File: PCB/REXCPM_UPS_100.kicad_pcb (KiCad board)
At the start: 2 copper layers, 51.3 x 18.3 mm, 11 parts, among them J1 Model_100_System_BUS, J2 SM04B, U1 742G02

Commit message: replace BAT54C with BAV170 to protect batteries better
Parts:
- D1: value BAT54C -> BAV170
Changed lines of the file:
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@@
   (title_block
     (title "REXCPM_UPS_100")
-    (date "2023-09-18")
-    (rev "005")
+    (date "2023-09-21")
+    (rev "006")
     (company "Brian K. White - b.kenyon.w@gmail.com")
     (comment 1 "github.com/bkw777/REXCPM_UPS")
@@
         (effects (font (size 0.8 0.8) (thickness 0.1)) (justify mirror))
     )
-    (fp_text value "BAT54C" (at 3 -1.3 90 unlocked) (layer "B.SilkS")
+    (fp_text value "BAV170" (at 3 -1.3 90 unlocked) (layer "B.SilkS")
         (effects (font (size 0.8 0.8) (thickness 0.1)) (justify mirror))
     )
@@
     (fp_arc (start 4.905239 -2.551328) (mid 4.8 -2.952056) (end 4.906989 -3.352321)
       (stroke (width 0.1) (type default)) (layer "B.SilkS"))
-    (fp_arc (start 5.224755 -1.996844) (mid 5.280899 -1.852058) (end 5.3 -1.697943)
+    (fp_arc (start 5.224755 -1.996844) (mid 5.280909 -1.852057) (end 5.3 -1.697943)
       (stroke (width 0.1) (type default)) (layer "B.SilkS"))
     (fp_line (start -6.35 -1.6375) (end -6.35 1.6375)
@@
     (fp_arc (start 4.905239 -2.551328) (mid 4.8 -2.952056) (end 4.906989 -3.352321)
       (stroke (width 0.1) (type default)) (layer "B.SilkS"))
-    (fp_arc (start 5.224755 -1.996844) (mid 5.280899 -1.852058) (end 5.3 -1.697943)
+    (fp_arc (start 5.224755 -1.996844) (mid 5.280909 -1.852057) (end 5.3 -1.697943)
       (stroke (width 0.1) (type default)) (layer "B.SilkS"))
     (fp_line (start -6.35 -1.6375) (end -6.35 1.6375)
@@
     (fp_arc (start 4.905239 -2.551328) (mid 4.8 -2.952056) (end 4.906989 -3.352321)
       (stroke (width 0.1) (type default)) (layer "B.SilkS"))
-    (fp_arc (start 5.224755 -1.996844) (mid 5.280899 -1.852058) (end 5.3 -1.697943)
+    (fp_arc (start 5.224755 -1.996844) (mid 5.280909 -1.852057) (end 5.3 -1.697943)
       (stroke (width 0.1) (type default)) (layer "B.SilkS"))
     (fp_line (start -6.35 -1.6375) (end -6.35 1.6375)
@@
     (fp_arc (start 4.905239 -2.551328) (mid 4.8 -2.952056) (end 4.906989 -3.352321)
       (stroke (width 0.1) (type default)) (layer "B.SilkS"))
-    (fp_arc (start 5.224755 -1.996844) (mid 5.280913 -1.852059) (end 5.3 -1.697943)
+    (fp_arc (start 5.224755 -1.996844) (mid 5.280899 -1.852058) (end 5.3 -1.697943)
       (stroke (width 0.1) (type default)) (layer "B.SilkS"))
     (fp_line (start -6.35 -1.6375) (end -6.35 1.6375)

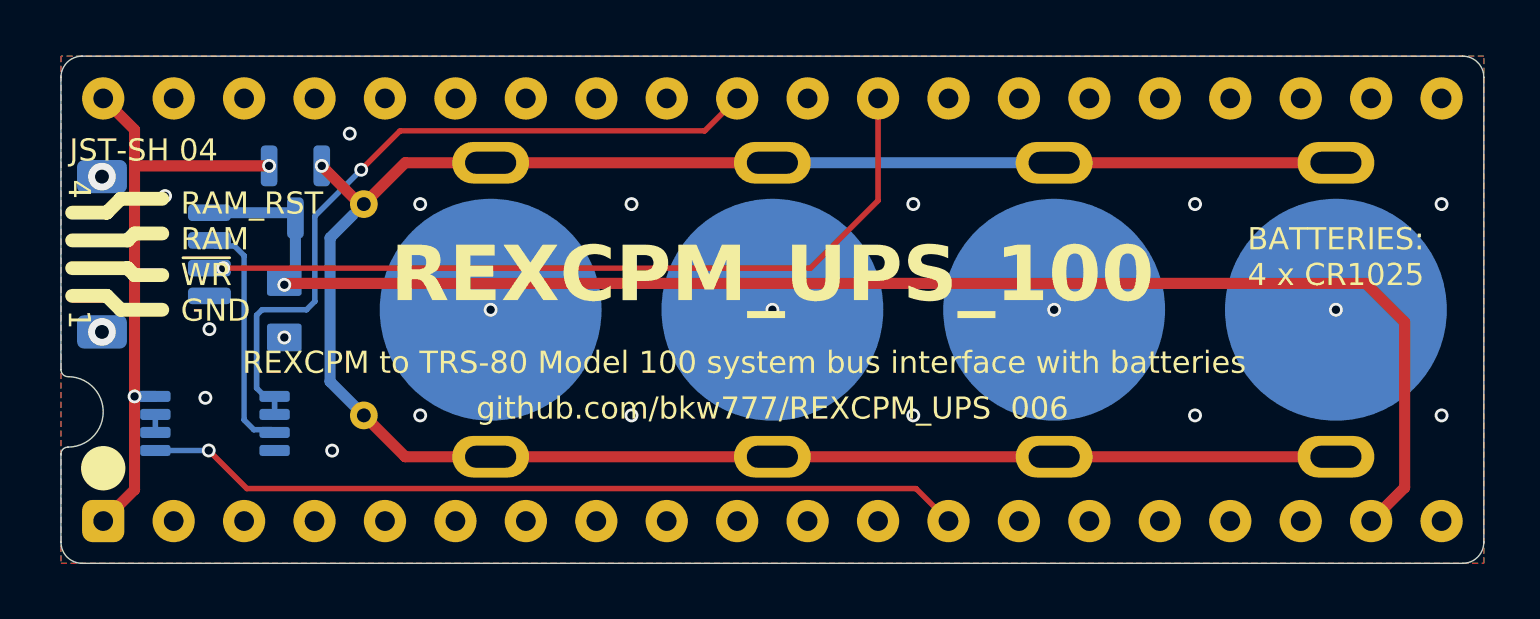
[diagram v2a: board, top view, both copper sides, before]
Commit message: m100 pcb routing, gnd, fiducials
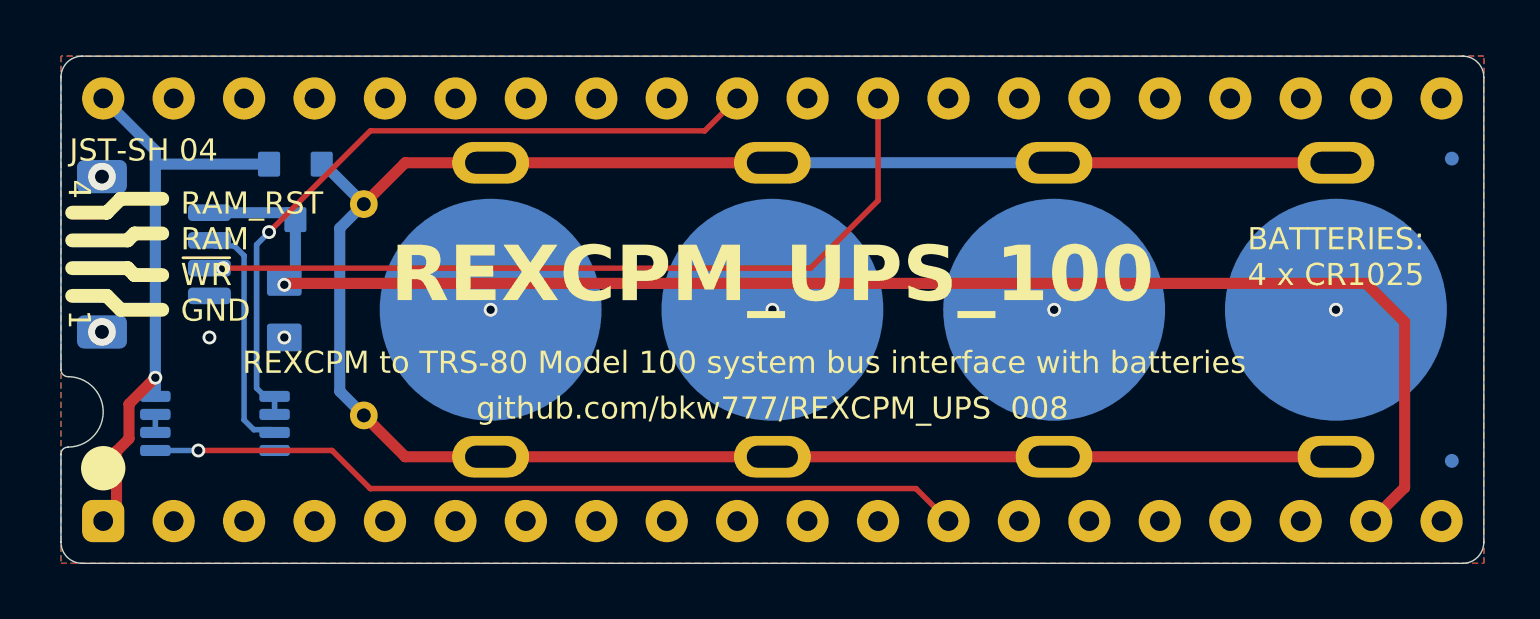
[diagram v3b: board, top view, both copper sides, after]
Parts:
- added REF**: Fiducial_0.5_1.0, 000_LOCAL:Fiducial_0.5_1.0, B.Cu at (112.6, 110.2)
- added REF**: Fiducial_0.5_1.0, 000_LOCAL:Fiducial_0.5_1.0, B.Cu at (161.0, 99.3)
- added REF**: Fiducial_0.5_1.0, 000_LOCAL:Fiducial_0.5_1.0, B.Cu at (161.0, 110.2)
- D1: footprint Package_TO_SOT_SMD:SOT-23 -> 000_LOCAL:SOT-23
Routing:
- net VBUS: track 21.8 -> 21.6 mm, vias 2 -> 1
- net /BATT+: track 81.6 -> 81.8 mm, vias 1 -> 0
- net GND: vias 22 -> 8
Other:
- board text removed: "CR1025"

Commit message: shield signals with ground pour
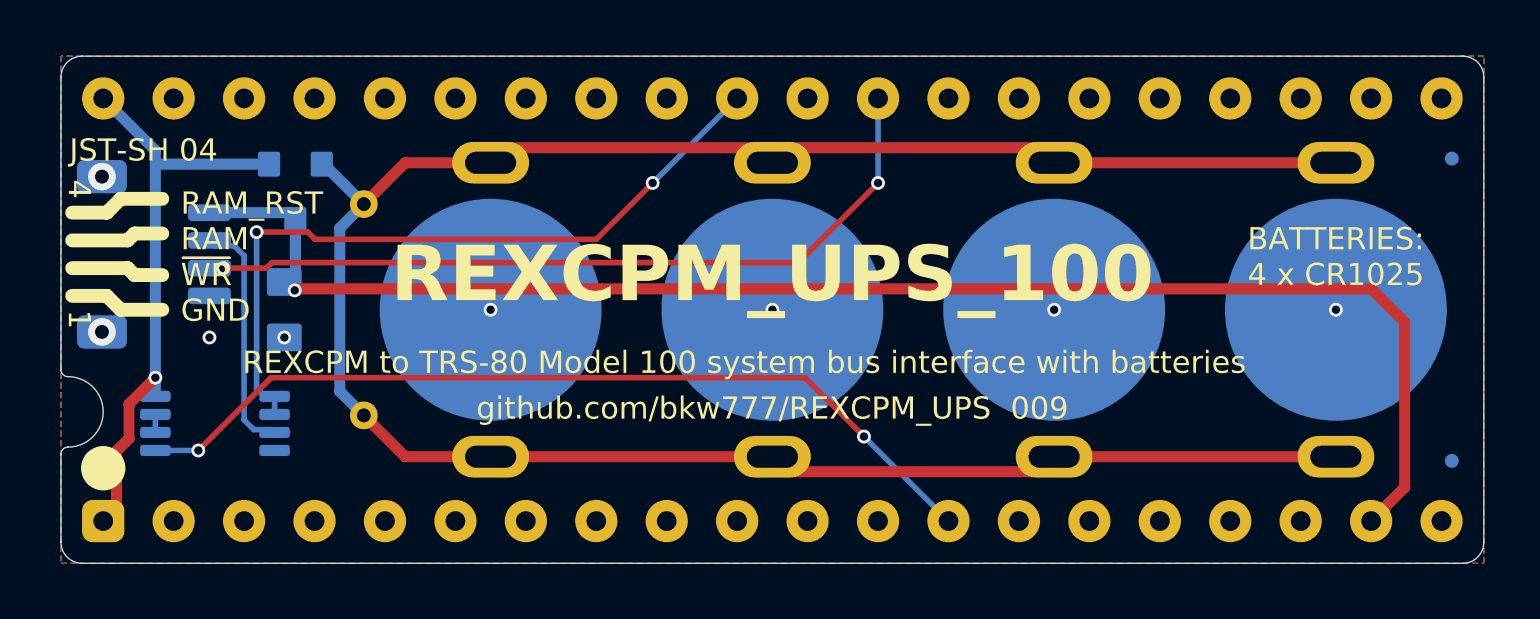
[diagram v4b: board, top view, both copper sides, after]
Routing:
- net /IO/~{M}: track 29.7 -> 31.8 mm, vias 1 -> 2
- net /BATT+: track 81.8 -> 83.1 mm
- net /A15: track 26.1 -> 26.6 mm, vias 1 -> 2
- net /~{WR}: track 28.8 -> 28.4 mm, vias 1 -> 2

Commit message: ground pour, routing, signal shielding
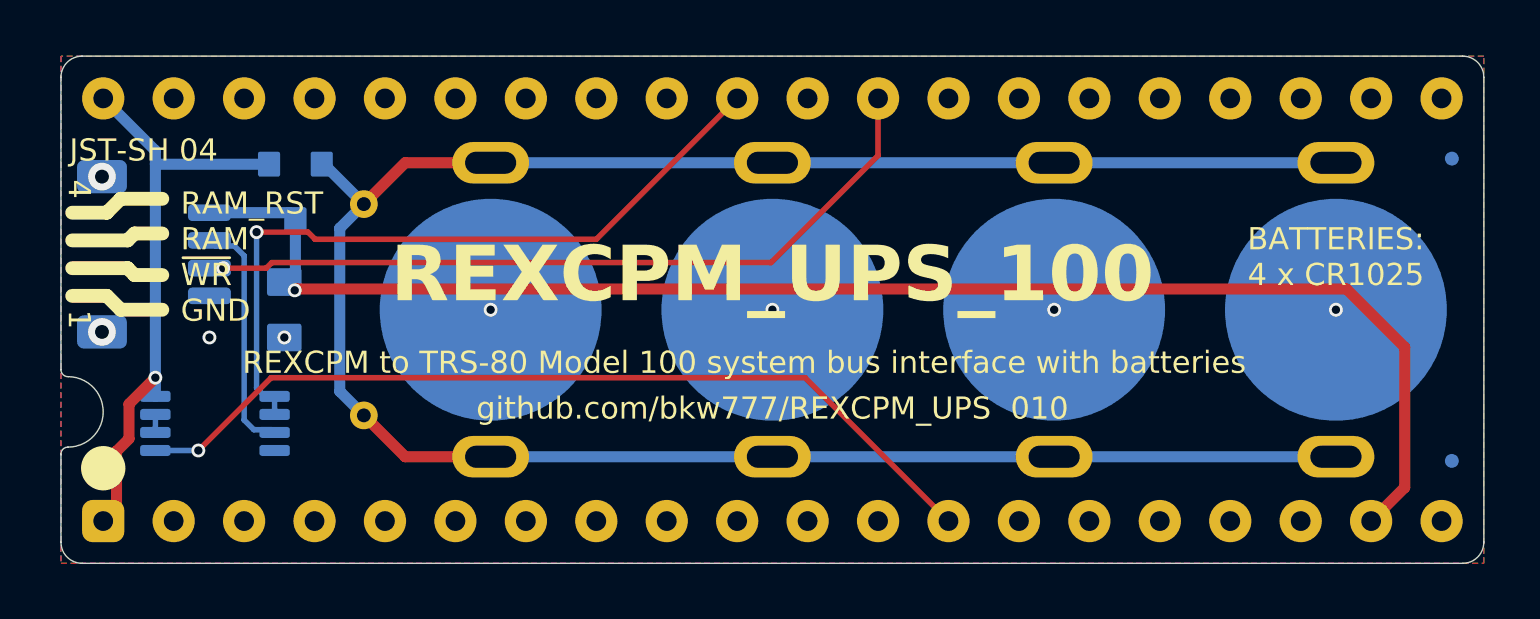
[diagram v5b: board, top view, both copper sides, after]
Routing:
- net /BATT+: track 83.1 -> 81.8 mm
- net /~{WR}: track 28.4 -> 27.9 mm, vias 2 -> 1
- net /RAM_RST: track 54.4 -> 53.8 mm
- net /IO/~{M}: vias 2 -> 1
- net /A15: vias 2 -> 1

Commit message: routing
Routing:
- net VBUS: vias 1 -> 3

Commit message: batt footprint
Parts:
- BT1, BT2, BT3, BT4: value Keystone_3031 -> BAT_3031
- J1: footprint 000_LOCAL:DIP-40_pins -> 000_LOCAL:DIP-40_PCB
- moved REF** 0.20 mm to (112.4, 110.2)
- moved REF** 0.10 mm to (161.1, 99.3)
- moved REF** 0.10 mm to (161.1, 110.2)
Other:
- outline, holes or cut-outs redrawn
- board text added: "BATTERIES 4 x CR1025"
- board text removed: "BATTERIES: 4 x CR1025"

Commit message: silkscreen
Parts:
- BT1, BT2, BT3, BT4: value BAT_3031 -> Keystone_3031
- U1: value 742G02 -> 2G02
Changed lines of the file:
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@@
   (title_block
     (title "REXCPM_UPS_100")
-    (date "2023-11-05")
-    (rev "011")
+    (date "2023-11-19")
+    (rev "012")
     (company "Brian K. White - b.kenyon.w@gmail.com")
     (comment 1 "github.com/bkw777/REXCPM_UPS")
@@
     (property "ki_keywords" "schottky diode common cathode")
     (attr smd)
-    (fp_text reference "D1" (at -0.8 -1.7 unlocked) (layer "B.SilkS")
+    (fp_text reference "D1" (at -1.25 -1.75 unlocked) (layer "B.SilkS")
         (effects (font (size 0.8 0.8) (thickness 0.1)) (justify right mirror))
     )
-    (fp_text value "BAV170" (at 0.75 -1.25 90 unlocked) (layer "B.SilkS")
+    (fp_text value "BAV170" (at -1.45 1.7 unlocked) (layer "B.SilkS")
         (effects (font (size 0.8 0.8) (thickness 0.1)) (justify left mirror))
     )
@@
     (property "ki_keywords" "connector")
     (attr smd)
-    (fp_text reference "J2" (at 2.5 2.6 180) (layer "B.SilkS")
-        (effects (font (size 0.8 0.8) (thickness 0.1)) (justify mirror))
-    )
-    (fp_text value "SM04B" (at 3.7 1.3 unlocked) (layer "B.SilkS")
+    (fp_text reference "J2" (at 0 -1.45 270) (layer "B.SilkS")
+        (effects (font (size 0.8 0.8) (thickness 0.1)) (justify mirror))
+    )
+    (fp_text value "SM04B" (at 0 0 90 unlocked) (layer "B.SilkS")
         (effects (font (size 0.8 0.8) (thickness 0.1)) (justify mirror))
     )
@@
         (effects (font (size 0.8 0.8) (thickness 0.1)) (justify mirror))
     )
-    (fp_text value "BAT_3031" (at 0 0) (layer "B.Fab")
+    (fp_text value "Keystone_3031" (at 0 0) (layer "B.Fab")
         (effects (font (size 1 1) (thickness 0.15)) (justify mirror))
     )
@@
     (property "ki_keywords" "Dual Gate NOR LVC CMOS")
     (attr smd)
-    (fp_text reference "U1" (at -3.5 1 unlocked) (layer "B.SilkS")
-        (effects (font (size 0.8 0.8) (thickness 0.1)) (justify mirror))
-    )
-    (fp_text value "742G02" (at -4 -1.7 180) (layer "B.SilkS")
-        (effects (font (size 0.8 0.8) (thickness 0.1)) (justify mirror))
+    (fp_text reference "U1" (at -0.7 -0.35 90 unlocked) (layer "B.SilkS")
+        (effects (font (size 0.8 0.8) (thickness 0.1)) (justify mirror))
+    )
+    (fp_text value "2G02" (at 0.75 0 90) (layer "B.SilkS")
+        (effects (font (size 0.8 0.7) (thickness 0.1)) (justify mirror))
     )
     (fp_text user "${REFERENCE}" (at 0 0) (layer "B.Fab")
@@
         (effects (font (size 0.8 0.8) (thickness 0.1)) (justify mirror))
     )
-    (fp_text value "BAT_3031" (at 0 0) (layer "B.Fab")
+    (fp_text value "Keystone_3031" (at 0 0) (layer "B.Fab")
         (effects (font (size 1 1) (thickness 0.15)) (justify mirror))
     )
@@
     (property "ki_keywords" "capacitor cap")
     (attr smd)
-    (fp_text reference "C1" (at -1.95 0 unlocked) (layer "B.SilkS")
-        (effects (font (size 0.8 0.8) (thickness 0.1)) (justify mirror))
-    )
-    (fp_text value "1u" (at 1.1 1.45 unlocked) (layer "B.SilkS")
+    (fp_text reference "C1" (at -1 -1.65 90 unlocked) (layer "B.SilkS")
+        (effects (font (size 0.8 0.8) (thickness 0.1)) (justify mirror))
+    )
+    (fp_text value "1u" (at 1 -1.65 90 unlocked) (layer "B.SilkS")
         (effects (font (size 0.8 0.8) (thickness 0.1)) (justify mirror))
     )
@@
         (effects (font (size 0.8 0.8) (thickness 0.1)) (justify mirror))
     )
-    (fp_text value "BAT_3031" (at 0 -6.35 90) (layer "B.Fab")
+    (fp_text value "Keystone_3031" (at 0 -6.35 90) (layer "B.Fab")
         (effects (font (size 1 1) (thickness 0.15)) (justify mirror))
     )
@@
         (effects (font (size 0.8 0.8) (thickness 0.1)) (justify mirror))
     )
-    (fp_text value "BAT_3031" (at 0 0) (layer "B.Fab")
-        (effects (font (size 1 1) (thickness 0.15)) (justify mirror))
-    )
+    (fp_text value "Keystone_3031" (at 0 0) (layer "B.Fab")
+        (effects (font (size 1 1) (thickness 0.15)) (justify mirror))
+    )
